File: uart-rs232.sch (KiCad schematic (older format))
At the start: 6 parts, among them U2201 MAX3232

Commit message: übergabe an 3ahel
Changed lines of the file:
@@
 $Descr A4 11693 8268
 encoding utf-8
-Sheet 22 27
+Sheet 27 27
 Title "RS-232 Sniffer"
-Date "2020-10-07"
+Date "2020-10-09"
 Rev "v20.0.0-dev"
 Comp "HTL-Steyr"
-Comment1 "Karl Zeilhofer"
+Comment1 "Prof. Karl Zeilhofer"
 Comment2 ""
 Comment3 ""
@@
 AR Path="/5F8AD0E2/5F7FE442/5F65EF92" Ref="U2601"  Part="1"
 AR Path="/5F8AD0E2/5F7FE44C/5F65EF92" Ref="U2701"  Part="1"
-F 0 "U2201" H 4850 4900 50  0000 C CNN
+AR Path="/5FA85ABF/5F7FE442/5F65EF92" Ref="U2602"  Part="1"
+AR Path="/5FA85ABF/5F7FE44C/5F65EF92" Ref="U2702"  Part="1"
+F 0 "U2702" H 4850 4900 50  0000 C CNN
 F 1 "MAX3232" H 4950 4800 50  0000 C CNN
 F 2 "Package_SO:SOIC-16_3.9x9.9mm_P1.27mm" H 5450 2650 50  0001 L CNN
@@
 AR Path="/5F8AD0E2/5F7FE442/5F65EF98" Ref="C2603"  Part="1"
 AR Path="/5F8AD0E2/5F7FE44C/5F65EF98" Ref="C2703"  Part="1"
-F 0 "C2203" H 6615 2996 50  0000 L CNN
+AR Path="/5FA85ABF/5F7FE442/5F65EF98" Ref="C2608"  Part="1"
+AR Path="/5FA85ABF/5F7FE44C/5F65EF98" Ref="C2708"  Part="1"
+F 0 "C2708" H 6615 2996 50  0000 L CNN
 F 1 "100n" H 6615 2905 50  0000 L CNN
 F 2 "Capacitor_SMD:C_0603_1608Metric" H 6538 2800 50  0001 C CNN
@@
 AR Path="/5F8AD0E2/5F7FE442/5F65EF9E" Ref="C2601"  Part="1"
 AR Path="/5F8AD0E2/5F7FE44C/5F65EF9E" Ref="C2701"  Part="1"
-F 0 "C2201" H 4465 2996 50  0000 L CNN
+AR Path="/5FA85ABF/5F7FE442/5F65EF9E" Ref="C2606"  Part="1"
+AR Path="/5FA85ABF/5F7FE44C/5F65EF9E" Ref="C2706"  Part="1"
+F 0 "C2706" H 4465 2996 50  0000 L CNN
 F 1 "100n" H 4465 2905 50  0000 L CNN
 F 2 "Capacitor_SMD:C_0603_1608Metric" H 4388 2800 50  0001 C CNN
@@
 AR Path="/5F8AD0E2/5F7FE442/5F65EFA4" Ref="C2605"  Part="1"
 AR Path="/5F8AD0E2/5F7FE44C/5F65EFA4" Ref="C2705"  Part="1"
-F 0 "C2205" V 6648 3300 50  0000 C CNN
+AR Path="/5FA85ABF/5F7FE442/5F65EFA4" Ref="C2610"  Part="1"
+AR Path="/5FA85ABF/5F7FE44C/5F65EFA4" Ref="C2710"  Part="1"
+F 0 "C2710" V 6648 3300 50  0000 C CNN
 F 1 "100n" V 6739 3300 50  0000 C CNN
 F 2 "Capacitor_SMD:C_0603_1608Metric" H 6938 3150 50  0001 C CNN
@@
 AR Path="/5F8AD0E2/5F7FE442/5F65EFAA" Ref="C2604"  Part="1"
 AR Path="/5F8AD0E2/5F7FE44C/5F65EFAA" Ref="C2704"  Part="1"
-F 0 "C2204" V 6348 3600 50  0000 C CNN
+AR Path="/5FA85ABF/5F7FE442/5F65EFAA" Ref="C2609"  Part="1"
+AR Path="/5FA85ABF/5F7FE44C/5F65EFAA" Ref="C2709"  Part="1"
+F 0 "C2709" V 6348 3600 50  0000 C CNN
 F 1 "100n" V 6439 3600 50  0000 C CNN
 F 2 "Capacitor_SMD:C_0603_1608Metric" H 6638 3450 50  0001 C CNN
@@
 AR Path="/5F8AD0E2/5F7FE442/5F65EFB3" Ref="#PWR02605"  Part="1"
 AR Path="/5F8AD0E2/5F7FE44C/5F65EFB3" Ref="#PWR02705"  Part="1"
-F 0 "#PWR02205" H 7250 3350 50  0001 C CNN
+AR Path="/5FA85ABF/5F7FE442/5F65EFB3" Ref="#PWR02610"  Part="1"
+AR Path="/5FA85ABF/5F7FE44C/5F65EFB3" Ref="#PWR02710"  Part="1"
+F 0 "#PWR02710" H 7250 3350 50  0001 C CNN
 F 1 "GND" V 7255 3472 50  0000 R CNN
 F 2 "" H 7250 3600 50  0001 C CNN
@@
 AR Path="/5F8AD0E2/5F7FE442/5F65EFB9" Ref="#PWR02604"  Part="1"
 AR Path="/5F8AD0E2/5F7FE44C/5F65EFB9" Ref="#PWR02704"  Part="1"
-F 0 "#PWR02204" H 7250 3050 50  0001 C CNN
+AR Path="/5FA85ABF/5F7FE442/5F65EFB9" Ref="#PWR02609"  Part="1"
+AR Path="/5FA85ABF/5F7FE44C/5F65EFB9" Ref="#PWR02709"  Part="1"
+F 0 "#PWR02709" H 7250 3050 50  0001 C CNN
 F 1 "GND" V 7255 3172 50  0000 R CNN
 F 2 "" H 7250 3300 50  0001 C CNN
@@
 AR Path="/5F8AD0E2/5F7FE442/5F65EFC4" Ref="C2602"  Part="1"
 AR Path="/5F8AD0E2/5F7FE44C/5F65EFC4" Ref="C2702"  Part="1"
-F 0 "C2202" V 5598 2300 50  0000 C CNN
+AR Path="/5FA85ABF/5F7FE442/5F65EFC4" Ref="C2607"  Part="1"
+AR Path="/5FA85ABF/5F7FE44C/5F65EFC4" Ref="C2707"  Part="1"
+F 0 "C2707" V 5598 2300 50  0000 C CNN
 F 1 "100n" V 5689 2300 50  0000 C CNN
 F 2 "Capacitor_SMD:C_0603_1608Metric" H 5888 2150 50  0001 C CNN
@@
 AR Path="/5F8AD0E2/5F7FE442/5F65EFCC" Ref="#PWR02603"  Part="1"
 AR Path="/5F8AD0E2/5F7FE44C/5F65EFCC" Ref="#PWR02703"  Part="1"
-F 0 "#PWR02203" H 6150 2050 50  0001 C CNN
+AR Path="/5FA85ABF/5F7FE442/5F65EFCC" Ref="#PWR02608"  Part="1"
+AR Path="/5FA85ABF/5F7FE44C/5F65EFCC" Ref="#PWR02708"  Part="1"
+F 0 "#PWR02708" H 6150 2050 50  0001 C CNN
 F 1 "GND" V 6155 2172 50  0000 R CNN
 F 2 "" H 6150 2300 50  0001 C CNN
@@
 AR Path="/5F8AD0E2/5F7FE442/5F65EFD3" Ref="#PWR02602"  Part="1"
 AR Path="/5F8AD0E2/5F7FE44C/5F65EFD3" Ref="#PWR02702"  Part="1"
-F 0 "#PWR02202" H 5400 4650 50  0001 C CNN
+AR Path="/5FA85ABF/5F7FE442/5F65EFD3" Ref="#PWR02607"  Part="1"
+AR Path="/5FA85ABF/5F7FE44C/5F65EFD3" Ref="#PWR02707"  Part="1"
+F 0 "#PWR02707" H 5400 4650 50  0001 C CNN
 F 1 "GND" H 5405 4727 50  0000 C CNN
 F 2 "" H 5400 4900 50  0001 C CNN
@@
 AR Path="/5F8AD0E2/5F7FE442/5F96E1EF" Ref="#PWR02601"  Part="1"
 AR Path="/5F8AD0E2/5F7FE44C/5F96E1EF" Ref="#PWR02701"  Part="1"
-F 0 "#PWR02201" H 5400 1950 50  0001 C CNN
+AR Path="/5FA85ABF/5F7FE442/5F96E1EF" Ref="#PWR02606"  Part="1"
+AR Path="/5FA85ABF/5F7FE44C/5F96E1EF" Ref="#PWR02706"  Part="1"
+F 0 "#PWR02706" H 5400 1950 50  0001 C CNN
 F 1 "+3V3" H 5415 2273 50  0000 C CNN
 F 2 "" H 5400 2100 50  0001 C CNN

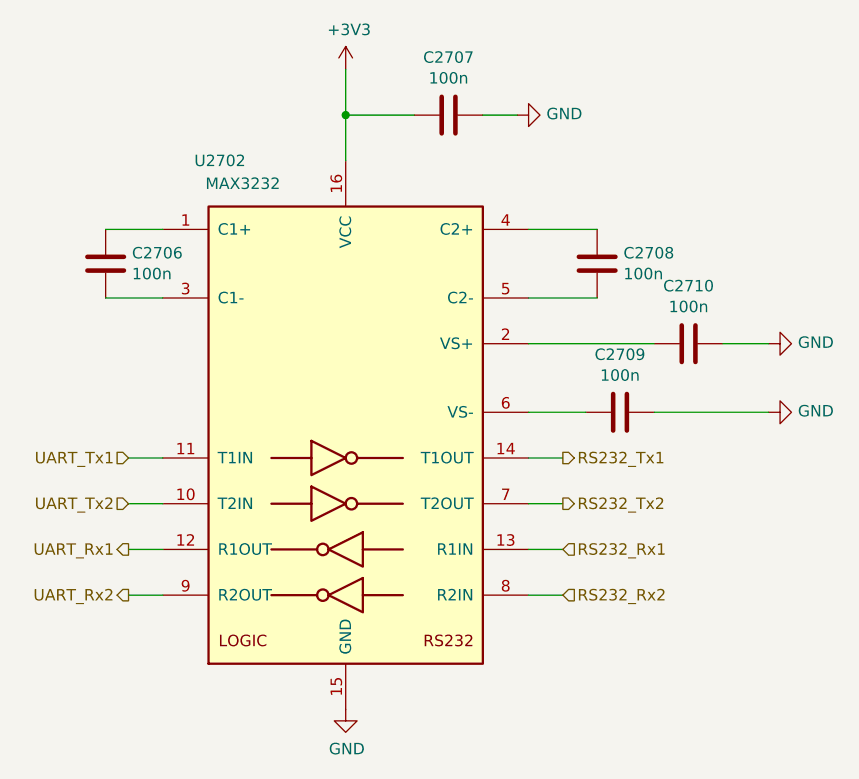
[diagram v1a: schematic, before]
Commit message: Layout fast fertig Footprint für 2x9-polig wurde aktualisiert
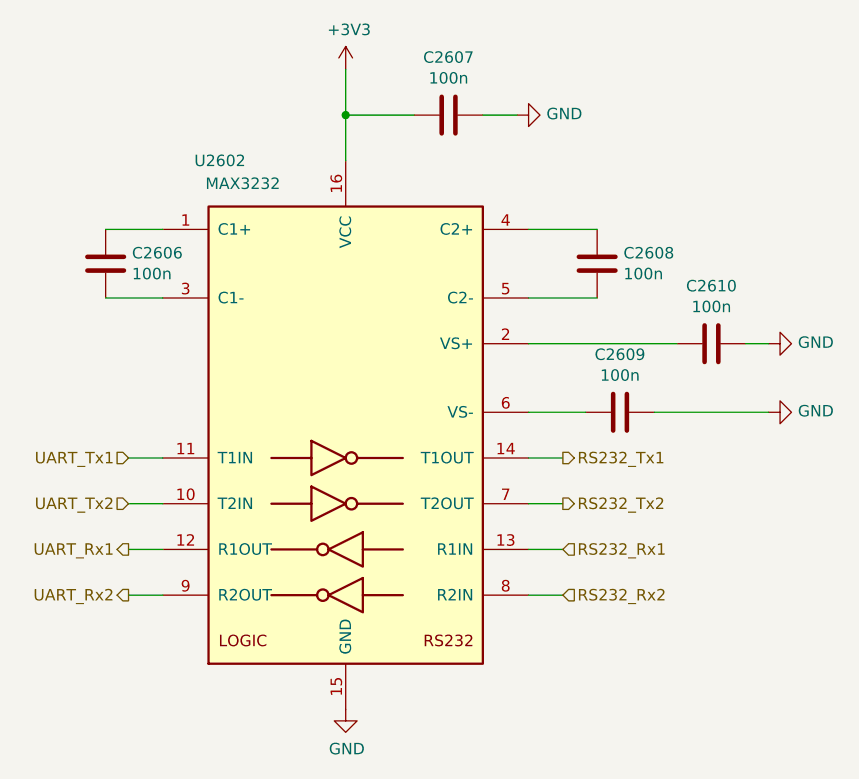
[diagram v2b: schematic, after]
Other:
- moved on the sheet: C2610
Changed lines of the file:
@@
 $Descr A4 11693 8268
 encoding utf-8
-Sheet 27 27
+Sheet 26 27
 Title "RS-232 Sniffer"
 Date "2020-10-09"
@@
 AR Path="/5FA85ABF/5F7FE442/5F65EF92" Ref="U2602"  Part="1"
 AR Path="/5FA85ABF/5F7FE44C/5F65EF92" Ref="U2702"  Part="1"
-F 0 "U2702" H 4850 4900 50  0000 C CNN
+F 0 "U2602" H 4850 4900 50  0000 C CNN
 F 1 "MAX3232" H 4950 4800 50  0000 C CNN
 F 2 "Package_SO:SOIC-16_3.9x9.9mm_P1.27mm" H 5450 2650 50  0001 L CNN
@@
 AR Path="/5FA85ABF/5F7FE442/5F65EF98" Ref="C2608"  Part="1"
 AR Path="/5FA85ABF/5F7FE44C/5F65EF98" Ref="C2708"  Part="1"
-F 0 "C2708" H 6615 2996 50  0000 L CNN
+F 0 "C2608" H 6615 2996 50  0000 L CNN
 F 1 "100n" H 6615 2905 50  0000 L CNN
 F 2 "Capacitor_SMD:C_0603_1608Metric" H 6538 2800 50  0001 C CNN
@@
 AR Path="/5FA85ABF/5F7FE442/5F65EF9E" Ref="C2606"  Part="1"
 AR Path="/5FA85ABF/5F7FE44C/5F65EF9E" Ref="C2706"  Part="1"
-F 0 "C2706" H 4465 2996 50  0000 L CNN
+F 0 "C2606" H 4465 2996 50  0000 L CNN
 F 1 "100n" H 4465 2905 50  0000 L CNN
 F 2 "Capacitor_SMD:C_0603_1608Metric" H 4388 2800 50  0001 C CNN
@@
 L Device:C C?
 U 1 1 5F65EFA4
-P 6900 3300
+P 7000 3300
 AR Path="/5F64F622/5F65CD72/5F65EFA4" Ref="C?"  Part="1"
 AR Path="/5F64F622/5F70BF21/5F65EFA4" Ref="C?"  Part="1"
@@
 AR Path="/5FA85ABF/5F7FE442/5F65EFA4" Ref="C2610"  Part="1"
 AR Path="/5FA85ABF/5F7FE44C/5F65EFA4" Ref="C2710"  Part="1"
-F 0 "C2710" V 6648 3300 50  0000 C CNN
-F 1 "100n" V 6739 3300 50  0000 C CNN
-F 2 "Capacitor_SMD:C_0603_1608Metric" H 6938 3150 50  0001 C CNN
-F 3 "https://datasheet.lcsc.com/szlcsc/1811151136_Walsin-Tech-Corp-0603B104K160CT_C80516.pdf" H 6900 3300 50  0001 C CNN
-F 4 "LCSC" H 6900 3300 50  0001 C CNN "Distributor"
-F 5 "Walsin Tech Corp" H 6900 3300 50  0001 C CNN "Manufacturer"
-F 6 "100nF ±10% 16V X7R" H 6900 3300 50  0001 C CNN "Notes"
-F 7 "" H 6900 3300 50  0001 C CNN "OrderNr"
-F 8 "" H 6900 3300 50  0001 C CNN "PartNr"
-F 9 "0.002141" H 6900 3300 50  0001 C CNN "PriceEUR"
-F 10 "500" H 6900 3300 50  0001 C CNN "PriceForQty"
-F 11 "https://lcsc.com/product-detail/Multilayer-Ceramic-Capacitors-MLCC-SMD-SMT_Walsin-Tech-Corp-0603B104K160CT_C80516.html" H 6900 3300 50  0001 C CNN "Weblink"
-F 12 "C80516" H 6900 3300 50  0001 C CNN "DistOrderNr"
-F 13 "0603B104K160CT" H 6900 3300 50  0001 C CNN "ManPartNr"
-	1    6900 3300
+F 0 "C2610" V 6748 3300 50  0000 C CNN
+F 1 "100n" V 6839 3300 50  0000 C CNN
+F 2 "Capacitor_SMD:C_0603_1608Metric" H 7038 3150 50  0001 C CNN
+F 3 "https://datasheet.lcsc.com/szlcsc/1811151136_Walsin-Tech-Corp-0603B104K160CT_C80516.pdf" H 7000 3300 50  0001 C CNN
+F 4 "LCSC" H 7000 3300 50  0001 C CNN "Distributor"
+F 5 "Walsin Tech Corp" H 7000 3300 50  0001 C CNN "Manufacturer"
+F 6 "100nF ±10% 16V X7R" H 7000 3300 50  0001 C CNN "Notes"
+F 7 "" H 7000 3300 50  0001 C CNN "OrderNr"
+F 8 "" H 7000 3300 50  0001 C CNN "PartNr"
+F 9 "0.002141" H 7000 3300 50  0001 C CNN "PriceEUR"
+F 10 "500" H 7000 3300 50  0001 C CNN "PriceForQty"
+F 11 "https://lcsc.com/product-detail/Multilayer-Ceramic-Capacitors-MLCC-SMD-SMT_Walsin-Tech-Corp-0603B104K160CT_C80516.html" H 7000 3300 50  0001 C CNN "Weblink"
+F 12 "C80516" H 7000 3300 50  0001 C CNN "DistOrderNr"
+F 13 "0603B104K160CT" H 7000 3300 50  0001 C CNN "ManPartNr"
+	1    7000 3300
 	0    1    1    0
 $EndComp
@@
 AR Path="/5FA85ABF/5F7FE442/5F65EFAA" Ref="C2609"  Part="1"
 AR Path="/5FA85ABF/5F7FE44C/5F65EFAA" Ref="C2709"  Part="1"
-F 0 "C2709" V 6348 3600 50  0000 C CNN
+F 0 "C2609" V 6348 3600 50  0000 C CNN
 F 1 "100n" V 6439 3600 50  0000 C CNN
 F 2 "Capacitor_SMD:C_0603_1608Metric" H 6638 3450 50  0001 C CNN
@@
 $EndComp
 Wire Wire Line
-	6200 3300 6750 3300
+	6200 3300 6850 3300
 Wire Wire Line
 	6200 3600 6450 3600
@@
 AR Path="/5FA85ABF/5F7FE442/5F65EFB3" Ref="#PWR02610"  Part="1"
 AR Path="/5FA85ABF/5F7FE44C/5F65EFB3" Ref="#PWR02710"  Part="1"
-F 0 "#PWR02710" H 7250 3350 50  0001 C CNN
+F 0 "#PWR02610" H 7250 3350 50  0001 C CNN
 F 1 "GND" V 7255 3472 50  0000 R CNN
 F 2 "" H 7250 3600 50  0001 C CNN
@@
 AR Path="/5FA85ABF/5F7FE442/5F65EFB9" Ref="#PWR02609"  Part="1"
 AR Path="/5FA85ABF/5F7FE44C/5F65EFB9" Ref="#PWR02709"  Part="1"
-F 0 "#PWR02709" H 7250 3050 50  0001 C CNN
+F 0 "#PWR02609" H 7250 3050 50  0001 C CNN
 F 1 "GND" V 7255 3172 50  0000 R CNN
 F 2 "" H 7250 3300 50  0001 C CNN
@@
 $EndComp
 Wire Wire Line
-	7050 3300 7250 3300
+	7150 3300 7250 3300
 Wire Wire Line
 	6200 3100 6500 3100
@@
 AR Path="/5FA85ABF/5F7FE442/5F65EFC4" Ref="C2607"  Part="1"
 AR Path="/5FA85ABF/5F7FE44C/5F65EFC4" Ref="C2707"  Part="1"
-F 0 "C2707" V 5598 2300 50  0000 C CNN
+F 0 "C2607" V 5598 2300 50  0000 C CNN
 F 1 "100n" V 5689 2300 50  0000 C CNN
 F 2 "Capacitor_SMD:C_0603_1608Metric" H 5888 2150 50  0001 C CNN
@@
 AR Path="/5FA85ABF/5F7FE442/5F65EFCC" Ref="#PWR02608"  Part="1"
 AR Path="/5FA85ABF/5F7FE44C/5F65EFCC" Ref="#PWR02708"  Part="1"
-F 0 "#PWR02708" H 6150 2050 50  0001 C CNN
+F 0 "#PWR02608" H 6150 2050 50  0001 C CNN
 F 1 "GND" V 6155 2172 50  0000 R CNN
 F 2 "" H 6150 2300 50  0001 C CNN
@@
 AR Path="/5FA85ABF/5F7FE442/5F65EFD3" Ref="#PWR02607"  Part="1"
 AR Path="/5FA85ABF/5F7FE44C/5F65EFD3" Ref="#PWR02707"  Part="1"
-F 0 "#PWR02707" H 5400 4650 50  0001 C CNN
+F 0 "#PWR02607" H 5400 4650 50  0001 C CNN
 F 1 "GND" H 5405 4727 50  0000 C CNN
 F 2 "" H 5400 4900 50  0001 C CNN
@@
 AR Path="/5FA85ABF/5F7FE442/5F96E1EF" Ref="#PWR02606"  Part="1"
 AR Path="/5FA85ABF/5F7FE44C/5F96E1EF" Ref="#PWR02706"  Part="1"
-F 0 "#PWR02706" H 5400 1950 50  0001 C CNN
+F 0 "#PWR02606" H 5400 1950 50  0001 C CNN
 F 1 "+3V3" H 5415 2273 50  0000 C CNN
 F 2 "" H 5400 2100 50  0001 C CNN
